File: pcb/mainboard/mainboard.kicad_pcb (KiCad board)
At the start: 2 copper layers, 100 x 100 mm, 10 parts, among them J2 SWD, U1 STM32G474RETx

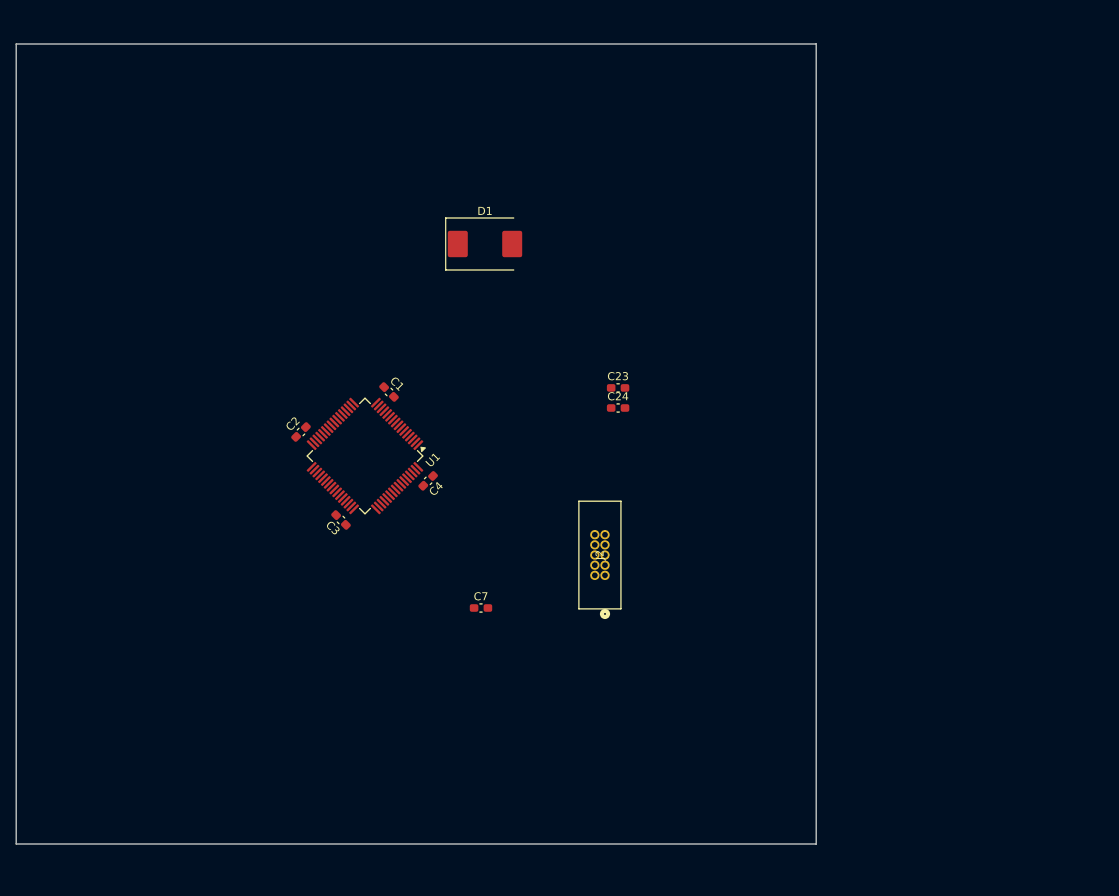
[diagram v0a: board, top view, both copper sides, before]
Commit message: Add TIP Voltage Control
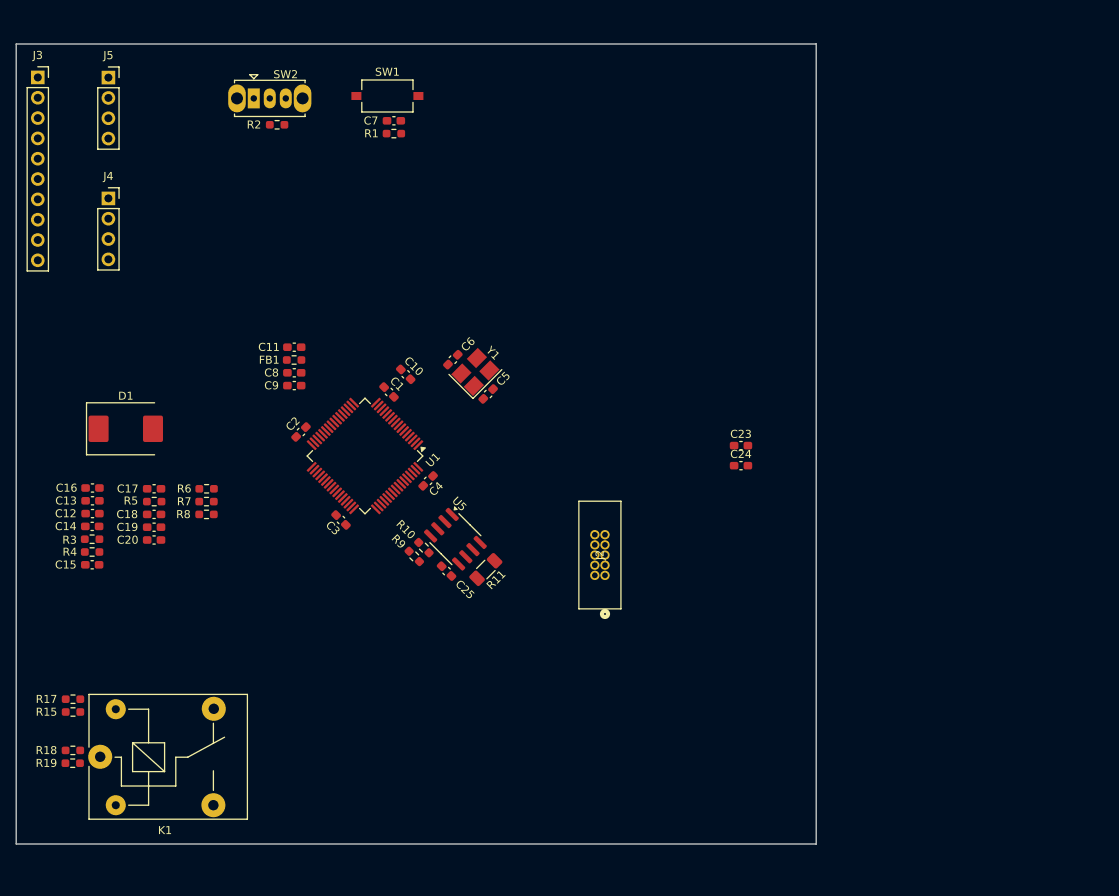
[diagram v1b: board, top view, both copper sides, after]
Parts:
- added C10: 4.7u, Capacitor_SMD:C_0603_1608Metric_Pad1.08x0.95mm_HandSolder, F.Cu at (98.7, 64.3)
- added C11: 1u, Capacitor_SMD:C_0603_1608Metric_Pad1.08x0.95mm_HandSolder, F.Cu at (84.8, 60.9)
- added C12: 4.7u, Capacitor_SMD:C_0603_1608Metric_Pad1.08x0.95mm_HandSolder, F.Cu at (59.5, 81.7)
- added C13: 4.7u, Capacitor_SMD:C_0603_1608Metric_Pad1.08x0.95mm_HandSolder, F.Cu at (59.5, 80.1)
- added C14: 0.01uF, Capacitor_SMD:C_0603_1608Metric_Pad1.08x0.95mm_HandSolder, F.Cu at (59.5, 83.3)
- added C15: 0.01u, Capacitor_SMD:C_0603_1608Metric_Pad1.08x0.95mm_HandSolder, F.Cu at (59.5, 88.1)
- added C16: 0.1u, Capacitor_SMD:C_0603_1608Metric_Pad1.08x0.95mm_HandSolder, F.Cu at (59.5, 78.5)
- added C17: 1000p, Capacitor_SMD:C_0603_1608Metric_Pad1.08x0.95mm_HandSolder, F.Cu at (67.2, 78.6)
- added C18: 47p, Capacitor_SMD:C_0603_1608Metric_Pad1.08x0.95mm_HandSolder, F.Cu at (67.2, 81.8)
- added C19: 47u, Capacitor_SMD:C_0603_1608Metric_Pad1.08x0.95mm_HandSolder, F.Cu at (67.2, 83.4)
- added C20: 47u, Capacitor_SMD:C_0603_1608Metric_Pad1.08x0.95mm_HandSolder, F.Cu at (67.2, 85.0)
- added C25: 100n, Capacitor_SMD:C_0603_1608Metric_Pad1.08x0.95mm_HandSolder, F.Cu at (103.8, 88.9)
- added C5: 10p, Capacitor_SMD:C_0603_1608Metric_Pad1.08x0.95mm_HandSolder, F.Cu at (109.0, 66.7)
- added C6: 10p, Capacitor_SMD:C_0603_1608Metric_Pad1.08x0.95mm_HandSolder, F.Cu at (104.6, 62.5)
- added C8: 10n, Capacitor_SMD:C_0603_1608Metric_Pad1.08x0.95mm_HandSolder, F.Cu at (84.8, 64.1)
- added C9: 1u, Capacitor_SMD:C_0603_1608Metric_Pad1.08x0.95mm_HandSolder, F.Cu at (84.8, 65.7)
- added FB1: 120R, Resistor_SMD:R_0603_1608Metric_Pad0.98x0.95mm_HandSolder, F.Cu at (84.7, 62.5)
- added J3: Conn_01x10, Connector_PinSocket_2.54mm:PinSocket_1x10_P2.54mm_Vertical, F.Cu at (52.7, 27.2)
- added J4: M1, Connector_PinSocket_2.54mm:PinSocket_1x04_P2.54mm_Vertical, F.Cu at (61.5, 42.3)
- added J5: M2, Connector_PinSocket_2.54mm:PinSocket_1x04_P2.54mm_Vertical, F.Cu at (61.5, 27.2)
- added K1: SANYOU_SRD_Form_C, Relay_THT:Relay_SPDT_SANYOU_SRD_Series_Form_C, F.Cu at (60.5, 112.1)
- added R1: 10k, Resistor_SMD:R_0603_1608Metric_Pad0.98x0.95mm_HandSolder, F.Cu at (97.2, 34.2)
- added R10: 10k, Resistor_SMD:R_0603_1608Metric_Pad0.98x0.95mm_HandSolder, F.Cu at (101.0, 86.0)
- added R11: 100, Resistor_SMD:R_1206_3216Metric_Pad1.30x1.75mm_HandSolder, F.Cu at (108.7, 88.7)
- added R15: 330R, Resistor_SMD:R_0603_1608Metric_Pad0.98x0.95mm_HandSolder, F.Cu at (57.1, 106.5)
- added R17: 10k, Resistor_SMD:R_0603_1608Metric_Pad0.98x0.95mm_HandSolder, F.Cu at (57.1, 104.9)
- added R18: 330R, Resistor_SMD:R_0603_1608Metric_Pad0.98x0.95mm_HandSolder, F.Cu at (57.1, 111.3)
- added R19: 10k, Resistor_SMD:R_0603_1608Metric_Pad0.98x0.95mm_HandSolder, F.Cu at (57.1, 112.9)
- added R2: 10k, Resistor_SMD:R_0603_1608Metric_Pad0.98x0.95mm_HandSolder, F.Cu at (82.6, 33.1)
- added R3: 332k, Resistor_SMD:R_0603_1608Metric_Pad0.98x0.95mm_HandSolder, F.Cu at (59.5, 84.9)
- added R4: 68.1k, Resistor_SMD:R_0603_1608Metric_Pad0.98x0.95mm_HandSolder, F.Cu at (59.5, 86.5)
- added R5: 29.4k, Resistor_SMD:R_0603_1608Metric_Pad0.98x0.95mm_HandSolder, F.Cu at (67.2, 80.2)
- added R6: 0, Resistor_SMD:R_0603_1608Metric_Pad0.98x0.95mm_HandSolder, F.Cu at (73.8, 78.6)
- added R7: 10.2k, Resistor_SMD:R_0603_1608Metric_Pad0.98x0.95mm_HandSolder, F.Cu at (73.8, 80.2)
- added R8: 3.24k, Resistor_SMD:R_0603_1608Metric_Pad0.98x0.95mm_HandSolder, F.Cu at (73.8, 81.8)
- added R9: 10k, Resistor_SMD:R_0603_1608Metric_Pad0.98x0.95mm_HandSolder, F.Cu at (99.8, 87.1)
- added SW1: RES_BUT, Button_Switch_SMD:SW_Tactile_SPST_NO_Straight_CK_PTS636Sx25SMTRLFS, F.Cu at (96.4, 29.5)
- added SW2: BOOT_SW, Button_Switch_THT:SW_Slide_SPDT_Straight_CK_OS102011MS2Q, F.Cu at (79.7, 29.8)
- added U5: INA219AxD, Package_SO:SOIC-8_3.9x4.9mm_P1.27mm, F.Cu at (104.9, 84.9)
- added Y1: 16MHz, Oscillator:Oscillator_SMD_Abracon_ASE-4Pin_3.2x2.5mm_HandSoldering, F.Cu at (107.4, 64.0)
- moved C7 61.9 mm to (97.2, 32.6), turned to 180 degrees
- moved D1 50.5 mm to (63.7, 71.1)
- moved C23 17.0 mm to (140.6, 73.2)
- moved C24 17.0 mm to (140.6, 75.7)
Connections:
- U1 pad 40: unconnected-(U1-PC8-Pad40) -> TIP_EN
- U1 pad 41: unconnected-(U1-PC9-Pad41) -> V_SELECT
- U1 pad 51: unconnected-(U1-PA15-Pad51) -> INA_SCL
- U1 pad 60: unconnected-(U1-PB7-Pad60) -> INA_SDA

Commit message: Create pcb
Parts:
- added G***: LOGO, Graphics:NaMi-logo, F.Cu at (123.4, 82.8)
- added H1: MountingHole, MountingHole:MountingHole_3.2mm_M3, F.Cu at (64.5, 28.2)
- added H2: MountingHole, MountingHole:MountingHole_3.2mm_M3, F.Cu at (147.8, 28.2)
- added H3: MountingHole, MountingHole:MountingHole_3.2mm_M3, F.Cu at (147.8, 94.2)
- added H4: MountingHole, MountingHole:MountingHole_3.2mm_M3, F.Cu at (64.5, 94.2)
- added J1: V_IN, TerminalBlock:CONN_395011002_MOL, F.Cu at (140.1, 27.2)
- added J7: TIP, TerminalBlock:CONN_395011002_MOL, F.Cu at (63.0, 83.8)
- added L1: 6.8u, Inductor_SMD:IND_IHLP-2525CZ_VIS-M, F.Cu at (126.5, 51.9)
- added Q1: NMOS, Package_TO_SOT_SMD:SOT-23_Handsoldering, F.Cu at (89.0, 91.0)
- added Q2: NMOS, Package_TO_SOT_SMD:SOT-23_Handsoldering, F.Cu at (76.8, 91.2)
- added U2: TPS54331DDA, Module:DDA8_3X2P13, F.Cu at (135.9, 47.4)
- added U3: TMC2208_SILENTSTEPSTICK, Connector:MODULE_TMC2208_SILENTSTEPSTICK, F.Cu at (74.1, 68.0)
- added U4: TMC2208_SILENTSTEPSTICK, Connector:MODULE_TMC2208_SILENTSTEPSTICK, F.Cu at (74.1, 43.8)
- moved C12 92.8 mm to (138.5, 33.0), turned to 180 degrees
- moved R3 92.3 mm to (141.5, 42.5), turned to 90 degrees
- moved C14 91.6 mm to (138.5, 37.0), turned to 180 degrees
- moved R4 91.3 mm to (139.5, 42.5), turned to -90 degrees
- moved C13 90.9 mm to (138.5, 35.0), turned to 180 degrees
- moved C15 90.4 mm to (137.5, 42.5), turned to 90 degrees
- moved C23 82.0 mm to (69.8, 32.0)
- moved C16 81.1 mm to (136.0, 51.5)
- moved SW2 78.9 mm to (145.0, 74.0), turned to 90 degrees
- moved R8 75.5 mm to (134.6, 37.0), turned to 180 degrees
- moved C18 73.0 mm to (129.0, 42.8), turned to 180 degrees
- moved C17 72.3 mm to (129.0, 41.0), turned to 180 degrees
- moved C24 72.1 mm to (71.1, 56.5)
- moved C19 71.6 mm to (127.4, 44.5)
- moved C20 71.5 mm to (127.4, 46.3)
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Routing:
- net +3.3V: track 0.00 -> 324.3 mm, vias 0 -> 15
- net +24V: track 0.00 -> 193.9 mm
- net GND: track 0.00 -> 131.1 mm, vias 0 -> 14
- net RESET: track 0.00 -> 81.2 mm
- net M_ENABLE: track 0.00 -> 78.0 mm, vias 0 -> 1
- net OLED_RESET: track 0.00 -> 49.0 mm
- net SWDIO: track 0.00 -> 46.7 mm
- net OLED_DC: track 0.00 -> 45.0 mm
- net INA_SDA: track 0.00 -> 44.8 mm, vias 0 -> 2
- net SWCLK: track 0.00 -> 43.5 mm
- net ENC_SIG_B: track 0.00 -> 41.0 mm
- net ENC_SIG_A: track 0.00 -> 40.6 mm
- net OLED_MOSI: track 0.00 -> 38.6 mm
- net TIP_IN: track 0.00 -> 38.4 mm
- net INA_SCL: track 0.00 -> 37.5 mm, vias 0 -> 2
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- added copper zone on F.Cu, net +24V
- added copper zone on F.Cu, net +3.3V
- added copper zone on B.Cu, net GND
- added copper zone on F.Cu, net GND
- added copper zone on F.Cu, net Net-(D1-K)
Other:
- board size 100 x 100 mm -> 94.2 x 77 mm
- board text added: "+24"
- board text added: "GND"
- board text added: "KN NaMi Tip Etcher v1.0 Adam Matysiak Jakub Klimkowski"

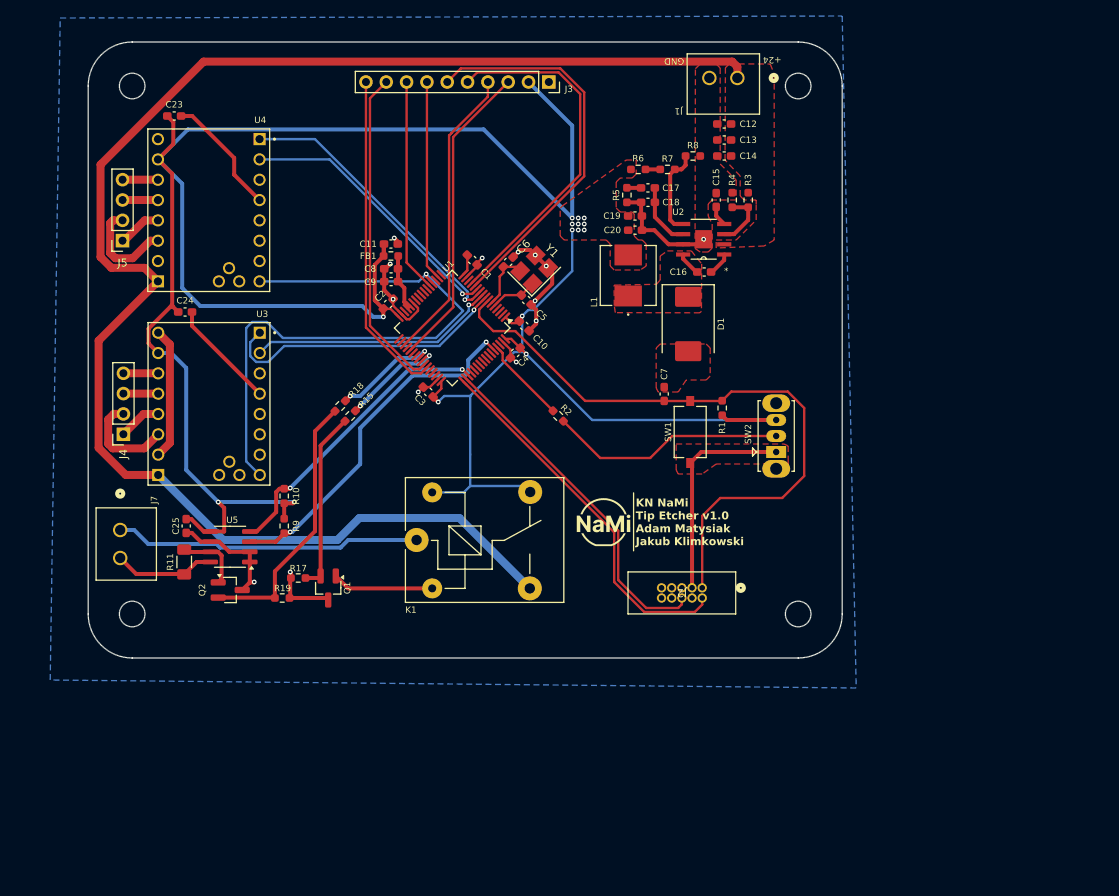
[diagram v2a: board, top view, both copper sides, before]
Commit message: Minor Schematic & Major PCB Rework
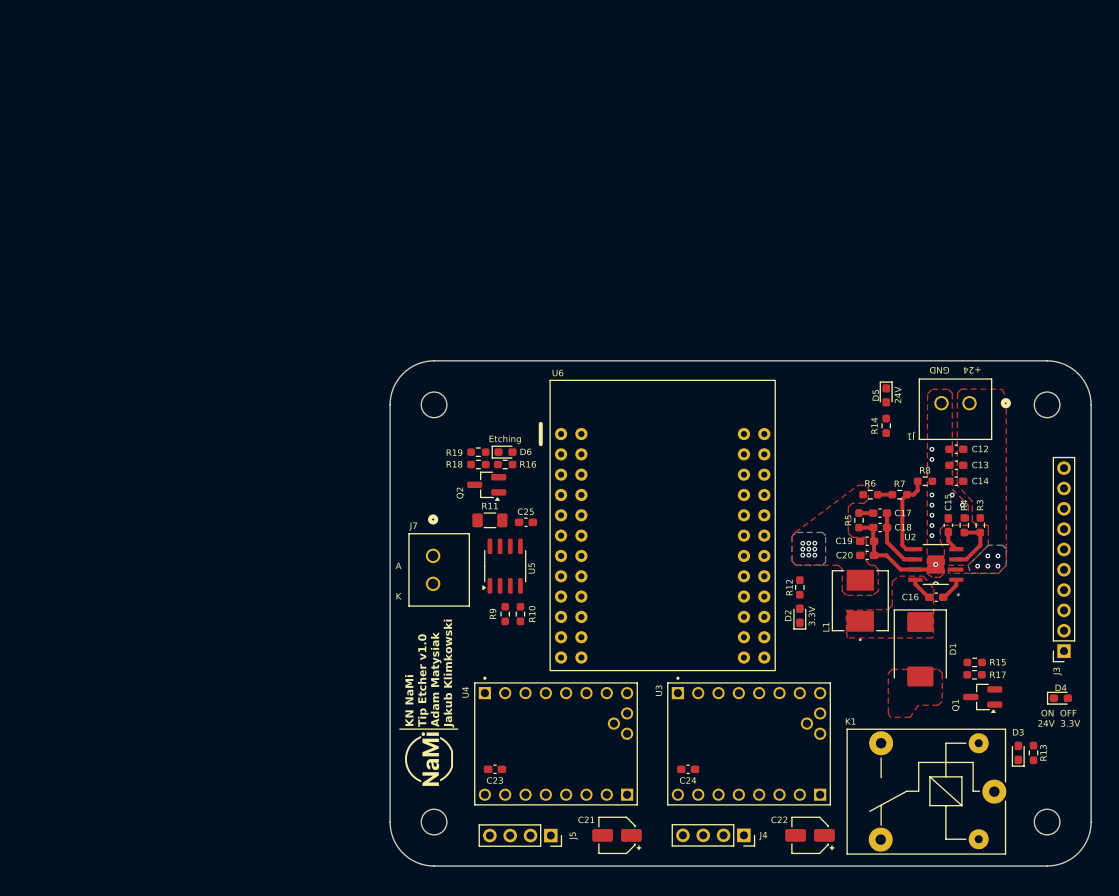
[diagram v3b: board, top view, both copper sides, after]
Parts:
- removed C1, C2, C3, C4, C7: 100n, Capacitor_SMD:C_0603_1608Metric_Pad1.08x0.95mm_HandSolder
- removed C10: 4.7u, Capacitor_SMD:C_0603_1608Metric_Pad1.08x0.95mm_HandSolder
- removed C11, C9: 1u, Capacitor_SMD:C_0603_1608Metric_Pad1.08x0.95mm_HandSolder
- removed C5, C6: 10p, Capacitor_SMD:C_0603_1608Metric_Pad1.08x0.95mm_HandSolder
- removed C8: 10n, Capacitor_SMD:C_0603_1608Metric_Pad1.08x0.95mm_HandSolder
- removed FB1: 120R, Resistor_SMD:R_0603_1608Metric_Pad0.98x0.95mm_HandSolder
- removed J2: SWD, Connector:CONN_3220-10-0100-00_CNC
- removed R1, R2: 10k, Resistor_SMD:R_0603_1608Metric_Pad0.98x0.95mm_HandSolder
- removed SW1: RES_BUT, Button_Switch_SMD:SW_Tactile_SPST_NO_Straight_CK_PTS636Sx25SMTRLFS
- removed SW2: BOOT_SW, Button_Switch_THT:SW_Slide_SPDT_Straight_CK_OS102011MS2Q
- removed U1: STM32G474RETx, Package_QFP:LQFP-64_10x10mm_P0.5mm
- removed Y1: 16MHz, Oscillator:Oscillator_SMD_Abracon_ASE-4Pin_3.2x2.5mm_HandSoldering
- added C21: 100n, Capacitor_SMD:CP_Elec_4x4.5, F.Cu at (125.1, 121.9)
- added C22: 100n, Capacitor_SMD:CP_Elec_4x4.5, F.Cu at (149.2, 121.9)
- added D2: LED, LED_SMD:LED_0603_1608Metric_Pad1.05x0.95mm_HandSolder, F.Cu at (148.0, 94.5)
- added D3: D, Diode_SMD:D_0603_1608Metric_Pad1.05x0.95mm_HandSolder, F.Cu at (175.3, 111.6)
- added D4: LED, LED_SMD:LED_0603_1608Metric_Pad1.05x0.95mm_HandSolder, F.Cu at (180.6, 104.8)
- added D5: LED, LED_SMD:LED_0603_1608Metric_Pad1.05x0.95mm_HandSolder, F.Cu at (158.8, 66.9)
- added D6: LED, LED_SMD:LED_0603_1608Metric_Pad1.05x0.95mm_HandSolder, F.Cu at (111.2, 74.0)
- added R12: R, Resistor_SMD:R_0603_1608Metric_Pad0.98x0.95mm_HandSolder, F.Cu at (148.0, 90.9)
- added R13: R, Resistor_SMD:R_0603_1608Metric_Pad0.98x0.95mm_HandSolder, F.Cu at (177.2, 111.6)
- added R14: R, Resistor_SMD:R_0603_1608Metric_Pad0.98x0.95mm_HandSolder, F.Cu at (158.8, 70.7)
- added R16: R, Resistor_SMD:R_0603_1608Metric_Pad0.98x0.95mm_HandSolder, F.Cu at (111.1, 75.6)
- added U6: STM32G474CoreBoard, STM32G474CoreBoard:STM32G474CoreBoard, F.Cu at (130.8, 84.5)
- J3: value Conn_01x10 -> Control Board
- moved J3 95.9 mm to (181.0, 98.9), turned to 180 degrees
- moved J4 92.4 mm to (141.0, 121.9), turned to -90 degrees
- moved J5 91.6 mm to (116.8, 121.9), turned to -90 degrees
- moved C23 91.0 mm to (109.9, 113.7), turned to 180 degrees
- moved R17 85.4 mm to (169.8, 101.8)
- moved C24 85.0 mm to (134.0, 113.7), turned to 180 degrees
- moved R15 83.9 mm to (169.8, 100.3), turned to 0 degrees
- moved Q1 82.9 mm to (170.8, 104.6), turned to 180 degrees
- moved U3 79.8 mm to (141.6, 110.5), turned to 90 degrees
- moved U4 79.6 mm to (117.5, 110.5), turned to 90 degrees
- moved K1 78.8 mm to (172.3, 116.5), turned to 180 degrees
- moved H1 54.9 mm to (102.2, 68.1)
- moved H2 50.6 mm to (178.9, 68.1)
- moved R5 49.9 mm to (155.3, 82.5)
- moved R7 49.9 mm to (160.4, 79.3)
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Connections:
- net Net-(D1-K) renamed /BUCK_3V3_PH
- net Net-(Q1-D) renamed /RELAY_OUT
- net Net-(U2-BOOT) renamed /BUCK_3V3_BOOT
- net Net-(U2-COMP) renamed /BUCK_3V3_COMP
- net Net-(U2-EN) renamed /BUCK_3V3_EN
- net Net-(U2-SS) renamed /BUCK_3V3_SS
- J4 pad 1: M1OA1 -> M1OA2
- J4 pad 2: M1OA2 -> M1OA1
- J5 pad 1: M2OA1 -> M2OA2
- J5 pad 2: M2OA2 -> M2OA1
- U3 pad JP2_2: Net-(U3-GND-PadJP2_2) -> GND
- U3 pad JP2_8: Net-(U3-GND-PadJP2_2) -> GND
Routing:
- net +3.3V: track 324.3 -> 0.00 mm, vias 15 -> 9
- net +24V: track 193.9 -> 0.00 mm, vias 0 -> 5
- net GND: track 131.1 -> 14.0 mm, vias 14 -> 10
- net RESET: track 81.2 -> 0.00 mm
- net M_ENABLE: track 78.0 -> 0.00 mm, vias 1 -> 0
- net OLED_RESET: track 49.0 -> 0.00 mm
- net SWDIO: track 46.7 -> 0.00 mm
- net OLED_DC: track 45.0 -> 0.00 mm
- net INA_SDA: track 44.8 -> 0.00 mm, vias 2 -> 0
- net SWCLK: track 43.5 -> 0.00 mm
- net ENC_SIG_B: track 41.0 -> 0.00 mm
- net ENC_SIG_A: track 40.6 -> 0.00 mm
- net OLED_MOSI: track 38.6 -> 0.00 mm
- net TIP_IN: track 38.4 -> 0.00 mm
- net INA_SCL: track 37.5 -> 0.00 mm, vias 2 -> 0
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- added copper zone on B.Cu, net +24V
- added copper zone on B.Cu, net +3.3V
- removed copper zone on B.Cu, net GND
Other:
- board size 94.2 x 77 mm -> 87.6 x 63.1 mm
- board text added: "24V"
- board text added: "3.3V"
- board text added: "A"
- board text added: "Etching"
- board text added: "K"
- board text added: "ON OFF 24V 3.3V"

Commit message: Update PCB
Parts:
- moved J7 77.5 mm to (178.8, 98.2), turned to 90 degrees
- moved J3 76.5 mm to (110.9, 68.1), turned to 90 degrees
- moved R19 69.9 mm to (176.0, 89.1), turned to 0 degrees
- moved R18 69.3 mm to (176.0, 87.6), turned to 0 degrees
- moved R9 66.9 mm to (172.7, 68.1), turned to -90 degrees
- moved Q2 66.5 mm to (175.0, 84.2), turned to 0 degrees
- moved R11 65.8 mm to (174.9, 79.8), turned to 180 degrees
- moved R10 63.4 mm to (170.8, 68.1), turned to -90 degrees
- moved D6 63.3 mm to (172.7, 89.2), turned to 180 degrees
- moved U5 63.2 mm to (172.7, 74.1), turned to -90 degrees
- moved R16 62.7 mm to (172.7, 87.6), turned to 180 degrees
- moved C25 56.5 mm to (170.1, 79.5), turned to 0 degrees
- moved G*** 51.5 mm to (142.5, 81.1)
- moved U6 10.0 mm to (121.1, 87.0), turned to 90 degrees
- moved R14 6.62 mm to (153.6, 66.5), turned to -90 degrees
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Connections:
- J3 pad 2: +3.3V -> OLED_3V3
- U6 pad 1: +3.3VA -> +3.3V
- U6 pad 2: +3.3VA -> +3.3V
- U6 pad 25: unconnected-(U6-3V3-Pad25) -> OLED_3V3
- U6 pad 26: unconnected-(U6-3V3-Pad26) -> OLED_3V3
- U6 pad 32: +3.3VA -> +3.3V
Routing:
- net +3.3V: track 0.00 -> 216.3 mm, vias 9 -> 10
- net +24V: track 0.00 -> 88.5 mm, vias 5 -> 6
- net ENC_SIG_B: track 0.00 -> 80.0 mm, vias 0 -> 1
- net ENC_SIG_A: track 0.00 -> 71.2 mm, vias 0 -> 1
- net TIP_EN: track 0.00 -> 63.8 mm
- net INA_SCL: track 0.00 -> 63.2 mm, vias 0 -> 1
- net INA_SDA: track 0.00 -> 58.3 mm, vias 0 -> 1
- net M_ENABLE: track 0.00 -> 56.5 mm
- net OLED_SCK: track 0.00 -> 51.7 mm, vias 0 -> 1
- net OLED_MOSI: track 0.00 -> 50.1 mm, vias 0 -> 1
- net V_SELECT: track 0.00 -> 44.9 mm
- net GND: track 14.0 -> 55.5 mm, vias 10 -> 22
- net DIR_2: track 0.00 -> 26.8 mm
- net STEP_2: track 0.00 -> 24.5 mm
- net TIP_IN: track 0.00 -> 21.7 mm
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- added copper zone on B.Cu, net GND
